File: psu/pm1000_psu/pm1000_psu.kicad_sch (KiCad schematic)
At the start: 42 parts, among them U1 LM317_TO-220, U2 LM317_TO-220, U3 LM317_TO-220

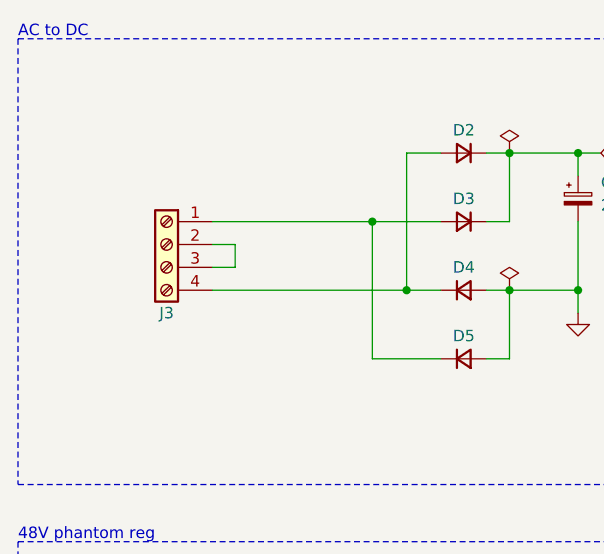
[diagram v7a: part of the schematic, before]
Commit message: psu schematic, add 5-terminal input with ground connection
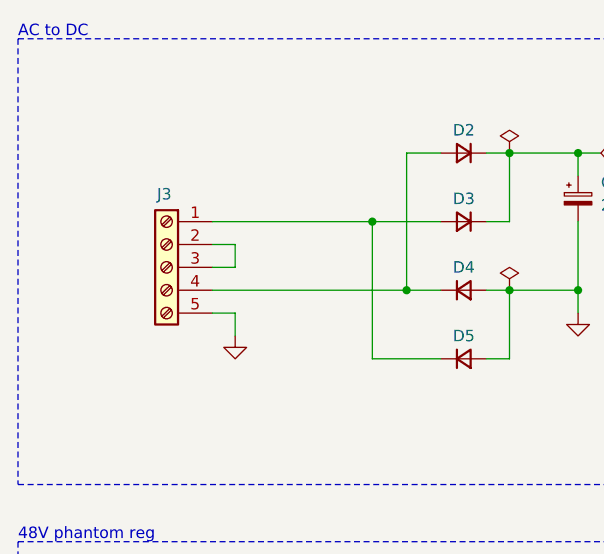
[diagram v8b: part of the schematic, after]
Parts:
- removed J3: (no value), TerminalBlock_Phoenix:TerminalBlock_Phoenix_PT-1,5-4-5.0-H_1x04_P5.00mm_Horizontal, symbol Connector:Screw_Terminal_01x04
- added J3: Screw_Terminal_01x05, symbol Connector:Screw_Terminal_01x05
- J1, J2, J4, J5: value (none) -> ~
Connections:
- net GND: now also J3.5 (Pin_5)
- net at D2.2 (A), D4.1 (K): now also J3.4 (Pin_4)
- net at D3.2 (A), D5.1 (K): now also J3.1 (Pin_1)
- new net: J3.2 (Pin_2), J3.3 (Pin_3)
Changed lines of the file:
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@@
 	(wire
 		(pts
+			(xy 45.72 52.07) (xy 45.72 54.61)
+		)
+		(stroke
+			(width 0)
+			(type default)
+		)
+	)
+	(wire
+		(pts
 			(xy 143.51 83.82) (xy 135.89 83.82)
 		)
@@
 	(wire
 		(pts
+			(xy 43.18 52.07) (xy 45.72 52.07)
+		)
+		(stroke
+			(width 0)
+			(type default)
+		)
+	)
+	(wire
+		(pts
 			(xy 64.77 105.41) (xy 64.77 111.76)
 		)
@@
 	)
 	(symbol
+		(lib_id "power:GND")
+		(at 45.72 54.61 0)
+		(unit 1)
+		(exclude_from_sim no)
+		(in_bom yes)
+		(on_board yes)
+		(dnp no)
+		(fields_autoplaced yes)
+		(property "Reference" "#PWR014"
+			(at 45.72 60.96 0)
+			(effects
+				(font
+					(size 1.27 1.27)
+				)
+				(hide yes)
+			)
+		)
+		(property "Value" "GND"
+			(at 45.72 59.69 0)
+			(effects
+				(font
+					(size 1.27 1.27)
+				)
+				(hide yes)
+			)
+		)
+		(property "Footprint" ""
+			(at 45.72 54.61 0)
+			(effects
+				(font
+					(size 1.27 1.27)
+				)
+				(hide yes)
+			)
+		)
+		(property "Datasheet" ""
+			(at 45.72 54.61 0)
+			(effects
+				(font
+					(size 1.27 1.27)
+				)
+				(hide yes)
+			)
+		)
+		(property "Description" ""
+			(at 45.72 54.61 0)
+			(effects
+				(font
+					(size 1.27 1.27)
+				)
+			)
+		)
+		(pin "1"
+		)
+		(instances
+			(project "pm1000_psu"
+				(path "/3a44f2ac-ebad-4a14-a75e-2fe0d50ab000"
+					(reference "#PWR014")
+					(unit 1)
+				)
+			)
+		)
+	)
+	(symbol
 		(lib_id "Device:C_Small")
 		(at 74.93 102.87 0)
@@
 	)
 	(symbol
-		(lib_id "Connector:Screw_Terminal_01x04")
-		(at 38.1 44.45 0)
-		(mirror y)
-		(unit 1)
-		(exclude_from_sim no)
-		(in_bom yes)
-		(on_board yes)
-		(dnp no)
-		(property "Reference" "J3"
-			(at 38.1 52.07 0)
-			(effects
-				(font
-					(size 1.27 1.27)
-				)
-			)
-		)
-		(property "Value" ""
-			(at 38.1 38.1 0)
-			(effects
-				(font
-					(size 1.27 1.27)
-				)
-				(hide yes)
-			)
-		)
-		(property "Footprint" "TerminalBlock_Phoenix:TerminalBlock_Phoenix_PT-1,5-4-5.0-H_1x04_P5.00mm_Horizontal"
-			(at 38.1 44.45 0)
-			(effects
-				(font
-					(size 1.27 1.27)
-				)
-				(hide yes)
-			)
-		)
-		(property "Datasheet" "~"
-			(at 38.1 44.45 0)
-			(effects
-				(font
-					(size 1.27 1.27)
-				)
-				(hide yes)
-			)
-		)
-		(property "Description" ""
-			(at 38.1 44.45 0)
-			(effects
-				(font
-					(size 1.27 1.27)
-				)
-			)
-		)
-		(property "Function" "Screw_Terminal_01x04"
-			(at 38.1 44.45 0)
-			(effects
-				(font
-					(size 1.27 1.27)
-				)
-				(hide yes)
-			)
-		)
-		(pin "1"
-		)
-		(pin "2"
-		)
-		(pin "3"
-		)
-		(pin "4"
-		)
-		(instances
-			(project ""
-				(path "/3a44f2ac-ebad-4a14-a75e-2fe0d50ab000"
-					(reference "J3")
-					(unit 1)
-				)
-			)
-		)
-	)
-	(symbol
 		(lib_id "Device:D_Small")
 		(at 146.05 27.94 0)
@@
 			)
 		)
-		(property "Value" ""
+		(property "Value" "~"
 			(at 194.31 90.17 0)
 			(effects
@@
 			)
 		)
-		(property "Value" ""
+		(property "Value" "~"
 			(at 91.44 91.44 0)
 			(effects
@@
 	)
 	(symbol
+		(lib_id "Connector:Screw_Terminal_01x05")
+		(at 38.1 46.99 0)
+		(mirror y)
+		(unit 1)
+		(exclude_from_sim no)
+		(in_bom yes)
+		(on_board yes)
+		(dnp no)
+		(property "Reference" "J3"
+			(at 37.846 38.862 0)
+			(effects
+				(font
+					(size 1.27 1.27)
+				)
+			)
+		)
+		(property "Value" "Screw_Terminal_01x05"
+			(at 38.1 55.88 0)
+			(effects
+				(font
+					(size 1.27 1.27)
+				)
+				(hide yes)
+			)
+		)
+		(property "Footprint" ""
+			(at 38.1 46.99 0)
+			(effects
+				(font
+					(size 1.27 1.27)
+				)
+				(hide yes)
+			)
+		)
+		(property "Datasheet" "~"
+			(at 38.1 46.99 0)
+			(effects
+				(font
+					(size 1.27 1.27)
+				)
+				(hide yes)
+			)
+		)
+		(property "Description" "Generic screw terminal, single row, 01x05, script generated (kicad-library-utils/schlib/autogen/connector/)"
+			(at 38.1 46.99 0)
+			(effects
+				(font
+					(size 1.27 1.27)
+				)
+				(hide yes)
+			)
+		)
+		(pin "5"
+		)
+		(pin "3"
+		)
+		(pin "2"
+		)
+		(pin "1"
+		)
+		(pin "4"
+		)
+		(instances
+			(project ""
+				(path "/3a44f2ac-ebad-4a14-a75e-2fe0d50ab000"
+					(reference "J3")
+					(unit 1)
+				)
+			)
+		)
+	)
+	(symbol
 		(lib_id "Device:R_Small")
 		(at 128.27 38.1 90)
@@
 			)
 		)
-		(property "Value" ""
+		(property "Value" "~"
 			(at 194.31 34.29 0)
 			(effects
@@
 			)
 		)
-		(property "Value" ""
+		(property "Value" "~"
 			(at 243.84 35.56 0)
 			(effects
